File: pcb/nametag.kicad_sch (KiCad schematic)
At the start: 0 parts

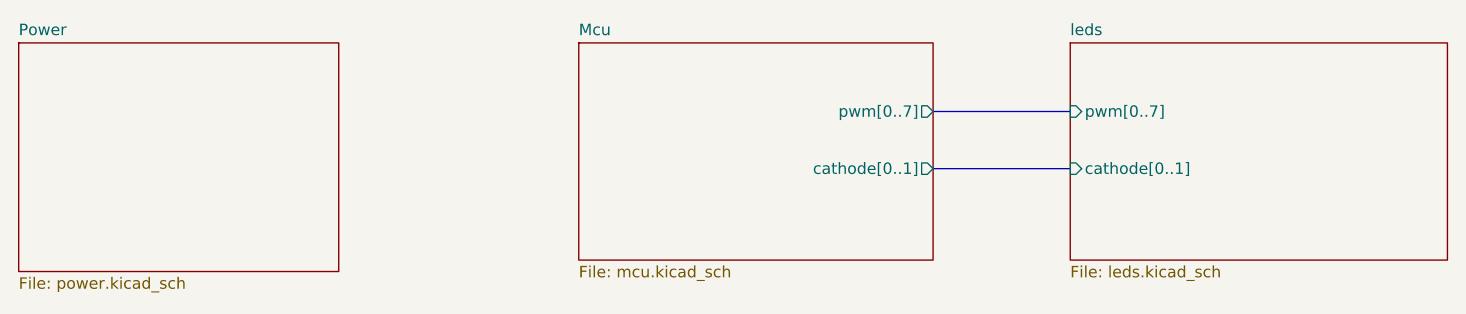
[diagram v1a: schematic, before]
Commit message: Update PCB with new naming of PWM channels
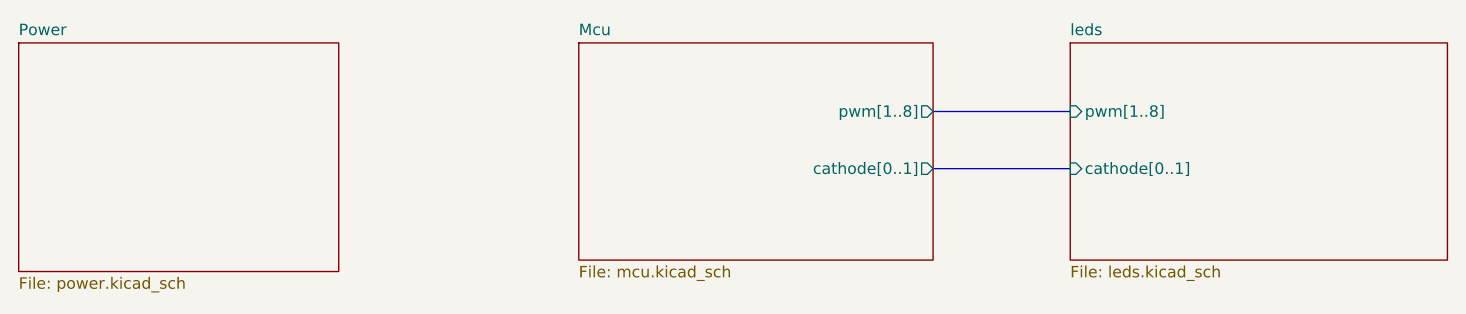
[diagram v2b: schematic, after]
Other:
- sheet Mcu ports: added pwm[1..8]; removed pwm[0..7]
- sheet leds ports: added pwm[1..8]; removed pwm[0..7]
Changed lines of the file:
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@@
 			)
 		)
-		(pin "pwm[0..7]" output
+		(pin "pwm[1..8]" output
 			(at 148.59 50.8 0)
 			(effects
@@
 			)
 		)
-		(pin "pwm[0..7]" input
+		(pin "pwm[1..8]" input
 			(at 163.83 50.8 180)
 			(effects
